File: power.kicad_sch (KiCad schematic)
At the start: 1 part, among them U5 INA226

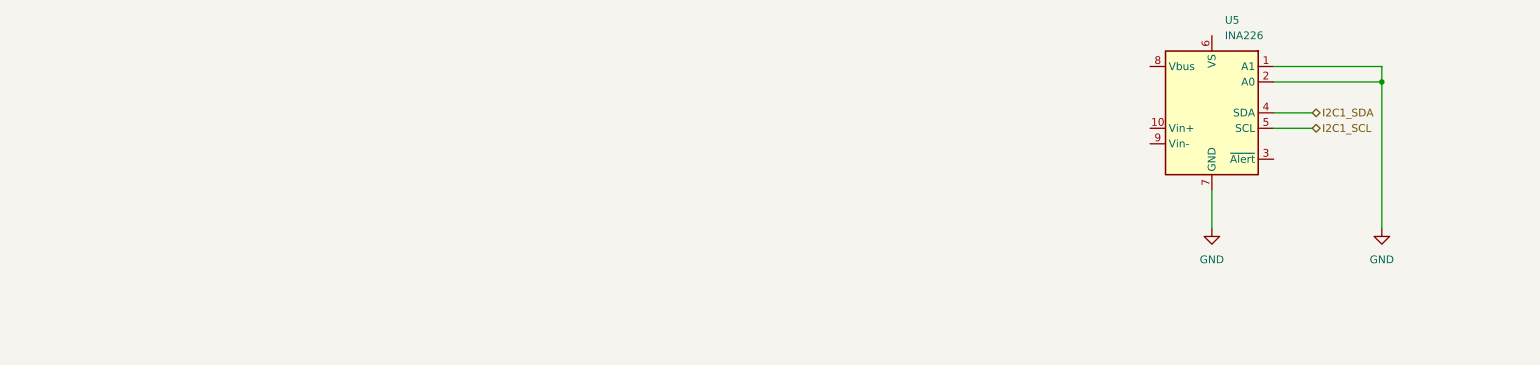
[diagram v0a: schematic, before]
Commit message: added main buck to step Vbat to 5V
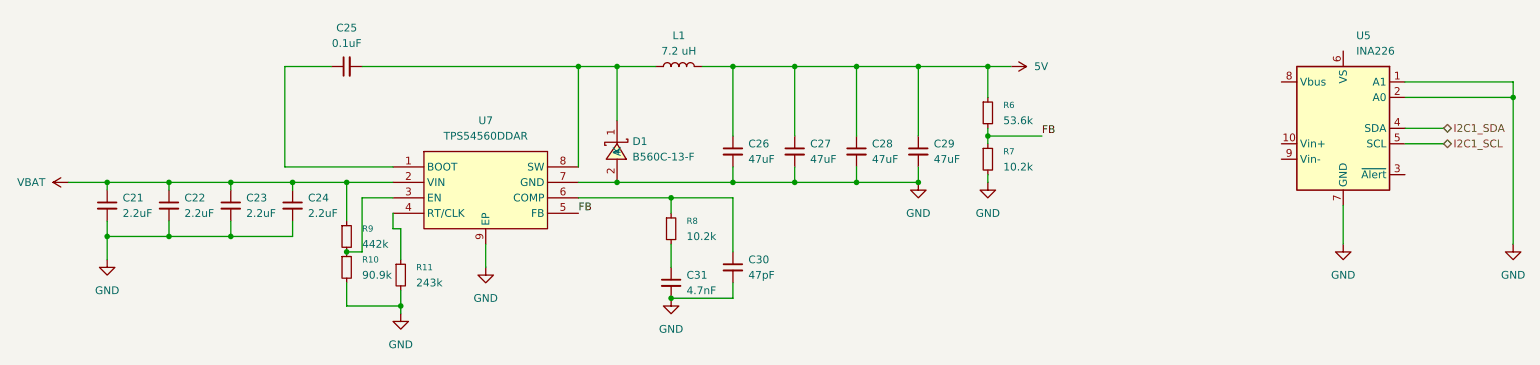
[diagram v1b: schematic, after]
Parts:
- added C21, C22, C23, C24: 2.2uF, Capacitor_SMD:C_0201_0603Metric_Pad0.64x0.40mm_HandSolder, symbol Device:C_Small
- added C25: 0.1uF, Capacitor_SMD:C_0201_0603Metric_Pad0.64x0.40mm_HandSolder, symbol Device:C_Small
- added C26, C27, C28, C29: 47uF, Capacitor_SMD:C_0201_0603Metric_Pad0.64x0.40mm_HandSolder, symbol Device:C_Small
- added C30: 47pF, Capacitor_SMD:C_0201_0603Metric_Pad0.64x0.40mm_HandSolder, symbol Device:C_Small
- added C31: 4.7nF, Capacitor_SMD:C_0201_0603Metric_Pad0.64x0.40mm_HandSolder, symbol Device:C_Small
- added D1: B560C-13-F, LCSC:SMC_L7.1-W6.2-LS8.1-RD, symbol LCSC:B560C-13-F
- added L1: 7.2 uH, Inductor_SMD:L_0201_0603Metric, symbol Device:L
- added R10: 90.9k, Resistor_SMD:R_0201_0603Metric, symbol Device:R_Small
- added R11: 243k, Resistor_SMD:R_0201_0603Metric, symbol Device:R_Small
- added R6: 53.6k, Resistor_SMD:R_0201_0603Metric, symbol Device:R_Small
- added R7, R8: 10.2k, Resistor_SMD:R_0201_0603Metric, symbol Device:R_Small
- added R9: 442k, Resistor_SMD:R_0201_0603Metric, symbol Device:R_Small
- added U7: TPS54560DDAR, LCSC:SOIC-8_L5.0-W4.0-P1.27-LS6.0-BL-EP2.0, symbol LCSC:TPS54560DDAR
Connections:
- net GND: now also C21.2, C22.2, C23.2, C24.2, C26.2, C27.2, C28.2, C29.2, C30.2, C31.2, D1.2 (A), R10.2, R11.2, R7.2, U7.7 (GND), U7.9 (EP)
- new net: C31.1, R8.2
- new net: C25.1, U7.1 (BOOT)
- new net: R10.1, R9.2, U7.3 (EN)
- new net: R11.1, U7.4 (RT/CLK)
- new net: C30.1, R8.1, U7.6 (COMP)
- new net: C25.2, D1.1 (K), L1.1, U7.8 (SW)
- new net 5V: C26.1, C27.1, C28.1, C29.1, L1.2, R6.1
- new net FB: R6.2, R7.1, U7.5 (FB)
- new net VBAT: C21.1, C22.1, C23.1, C24.1, R9.1, U7.2 (VIN)
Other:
- moved on the sheet: U5

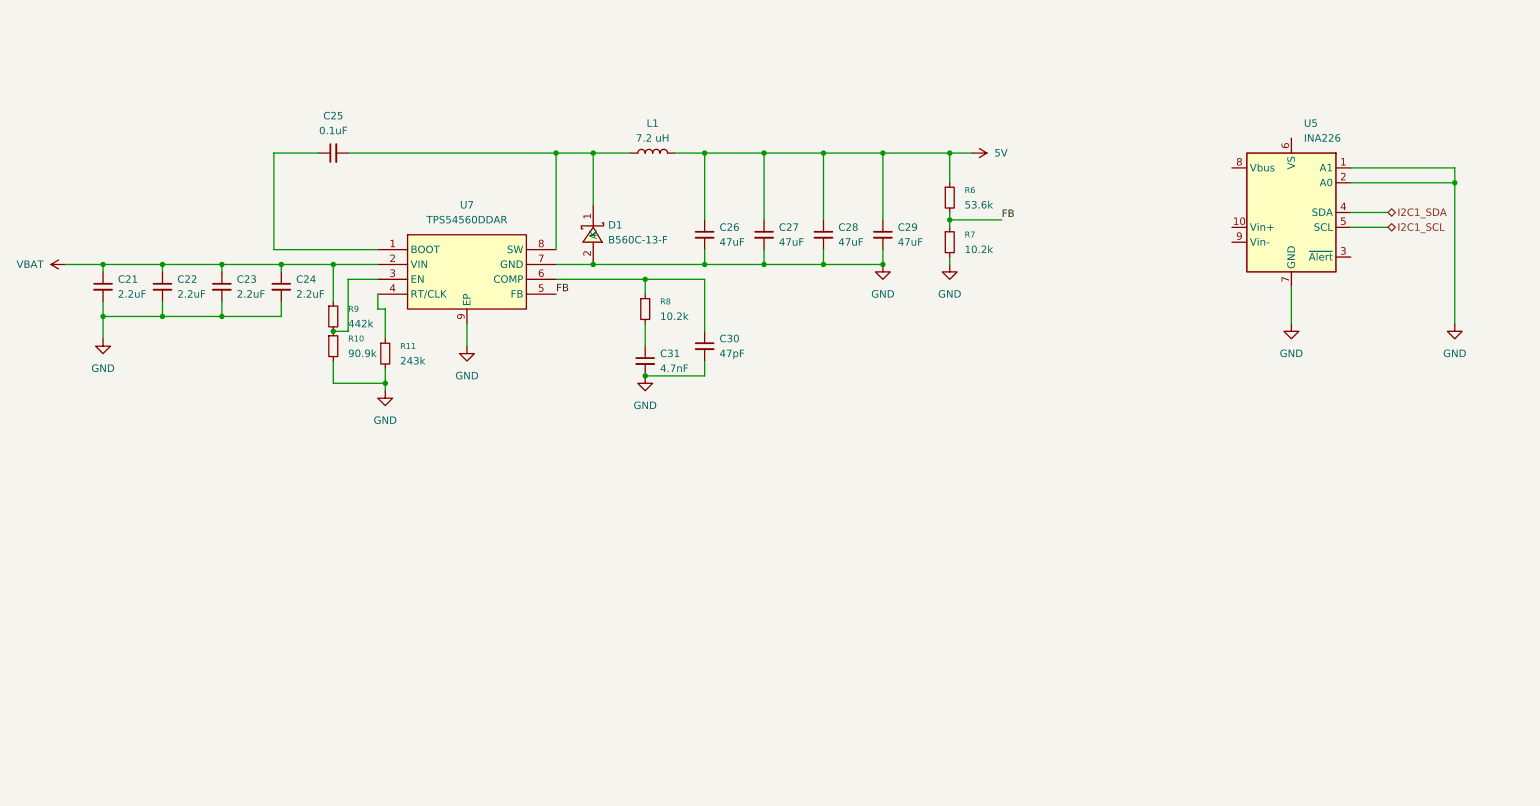
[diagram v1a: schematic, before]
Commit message: added in power converters being LDOs for the sensors and the MCU seperate
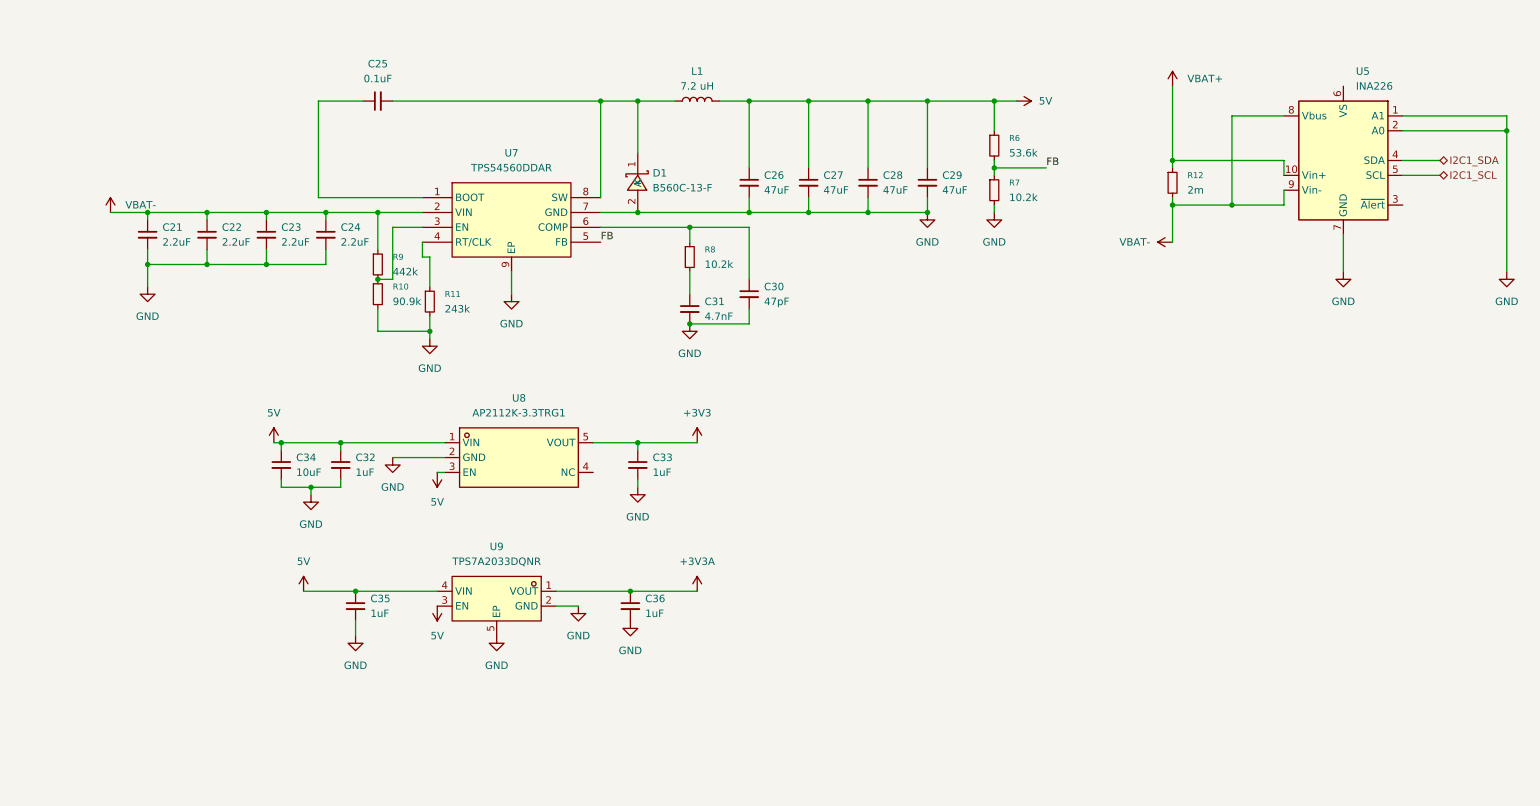
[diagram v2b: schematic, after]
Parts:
- added C32, C33, C35, C36: 1uF, Capacitor_SMD:C_0201_0603Metric_Pad0.64x0.40mm_HandSolder, symbol Device:C_Small
- added C34: 10uF, Capacitor_SMD:C_0201_0603Metric_Pad0.64x0.40mm_HandSolder, symbol Device:C_Small
- added R12: 2m, Resistor_SMD:R_0201_0603Metric, symbol Device:R_Small
- added U8: AP2112K-3.3TRG1, LCSC:SOT-25-5_L2.9-W1.6-P0.95-LS2.8-BL, symbol LCSC:AP2112K-3.3TRG1
- added U9: TPS7A2033DQNR, LCSC:UDFN-4_L1.0-W1.0-P0.65-TL, symbol LCSC:TPS7A2033DQNR
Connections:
- net VBAT is gone; now on net VBAT-: C21.1, C22.1, C23.1, C24.1, R9.1, U7.2 (VIN)
- net 5V: now also C32.1, C34.1, C35.1, U8.1 (VIN), U8.3 (EN), U9.3 (EN), U9.4 (VIN)
- net GND: now also C32.2, C33.2, C34.2, C35.2, C36.2, U8.2 (GND), U9.2 (GND), U9.5 (EP)
- net VBAT+: now reaches U5.10 (Vin+)
- net VBAT+: now also R12.1
- net VBAT-: now reaches U5.8 (Vbus)
- net VBAT-: now also U5.9 (Vin-), R12.2
- new net +3V3: C33.1, U8.5 (VOUT)
- new net +3V3A: C36.1, U9.1 (VOUT)
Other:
- moved on the sheet: C21, C22, C23, C24, C25, C26, C27, C28, C29, C30, C31, D1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

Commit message: Added new connector types for future connections later
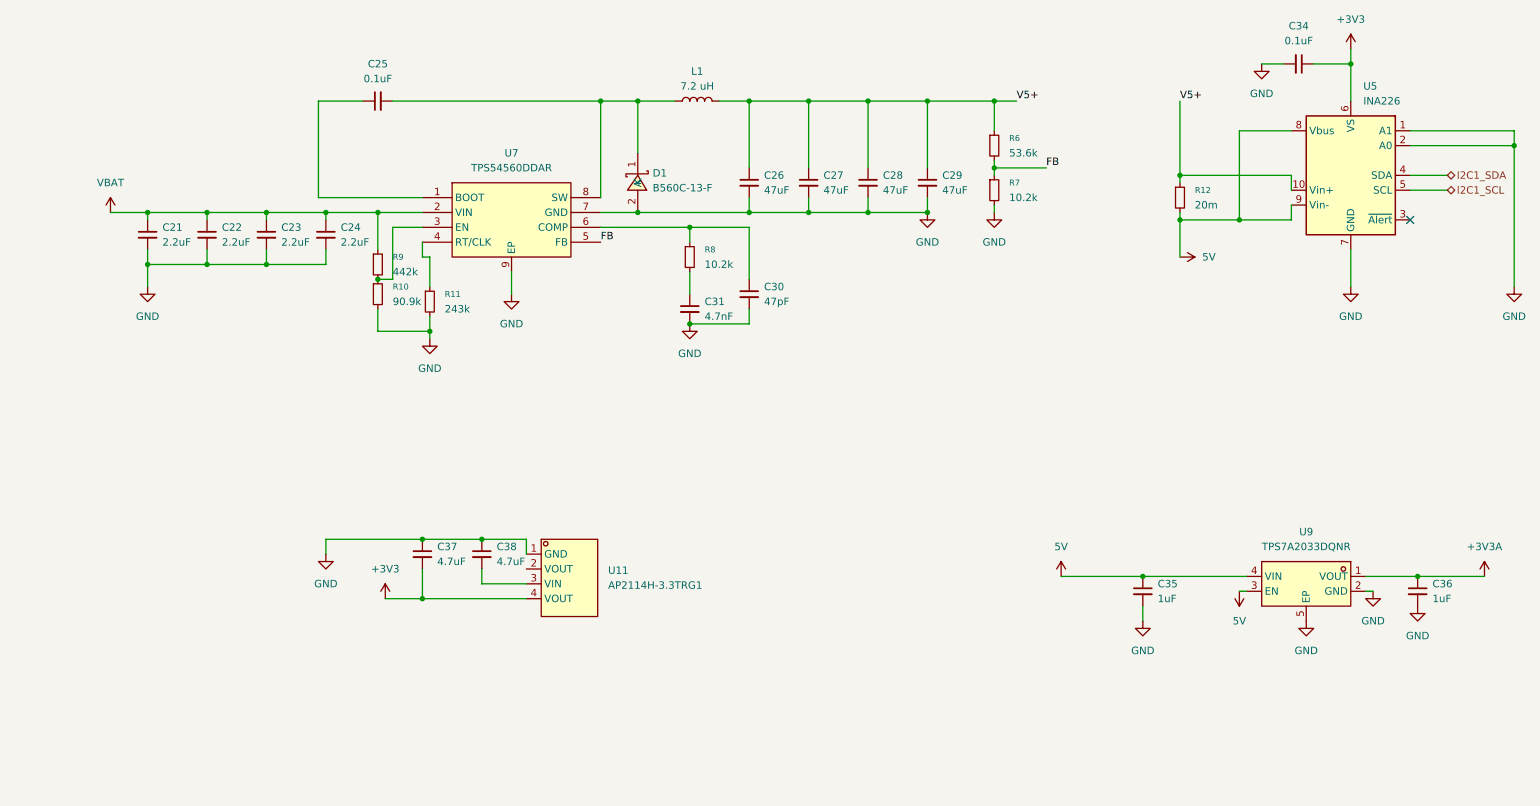
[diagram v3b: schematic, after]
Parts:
- removed C32, C33: 1uF, Capacitor_SMD:C_0201_0603Metric_Pad0.64x0.40mm_HandSolder, symbol Device:C_Small
- removed U8: AP2112K-3.3TRG1, LCSC:SOT-25-5_L2.9-W1.6-P0.95-LS2.8-BL, symbol LCSC:AP2112K-3.3TRG1
- added C37, C38: 4.7uF, Capacitor_SMD:C_0201_0603Metric_Pad0.64x0.40mm_HandSolder, symbol Device:C_Small
- added U11: AP2114H-3.3TRG1, LCSC:SOT-223_L6.7-W3.5-P2.30-BR, symbol LCSC:AP2114H-3.3TRG1
- C34: value 10uF -> 0.1uF
- R12: value 2m -> 20m
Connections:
- net +3V3: now also C34.1, U5.6 (VS), C37.2, U11.4 (VOUT)
- net 5V: now also R12.2, U5.8 (Vbus), U5.9 (Vin-); no longer C26.1, C27.1, C28.1, C29.1, C34.1, L1.2, R6.1
- net GND: now also C37.1, C38.1, U11.1 (GND)
- net VBAT+ renamed V5+
- net V5+: now also C26.1, C27.1, C28.1, C29.1, L1.2, R6.1
- net VBAT- renamed VBAT
- net VBAT: no longer R12.2, U5.8 (Vbus), U5.9 (Vin-)
- new net: C38.2, U11.3 (VIN)
- no-connect marks 0 -> 1
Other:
- moved on the sheet: C35, C36, R12, U5, U9

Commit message: mainly added usart 3, uart 4, and I2C3 connections and planning to add a CAN connection
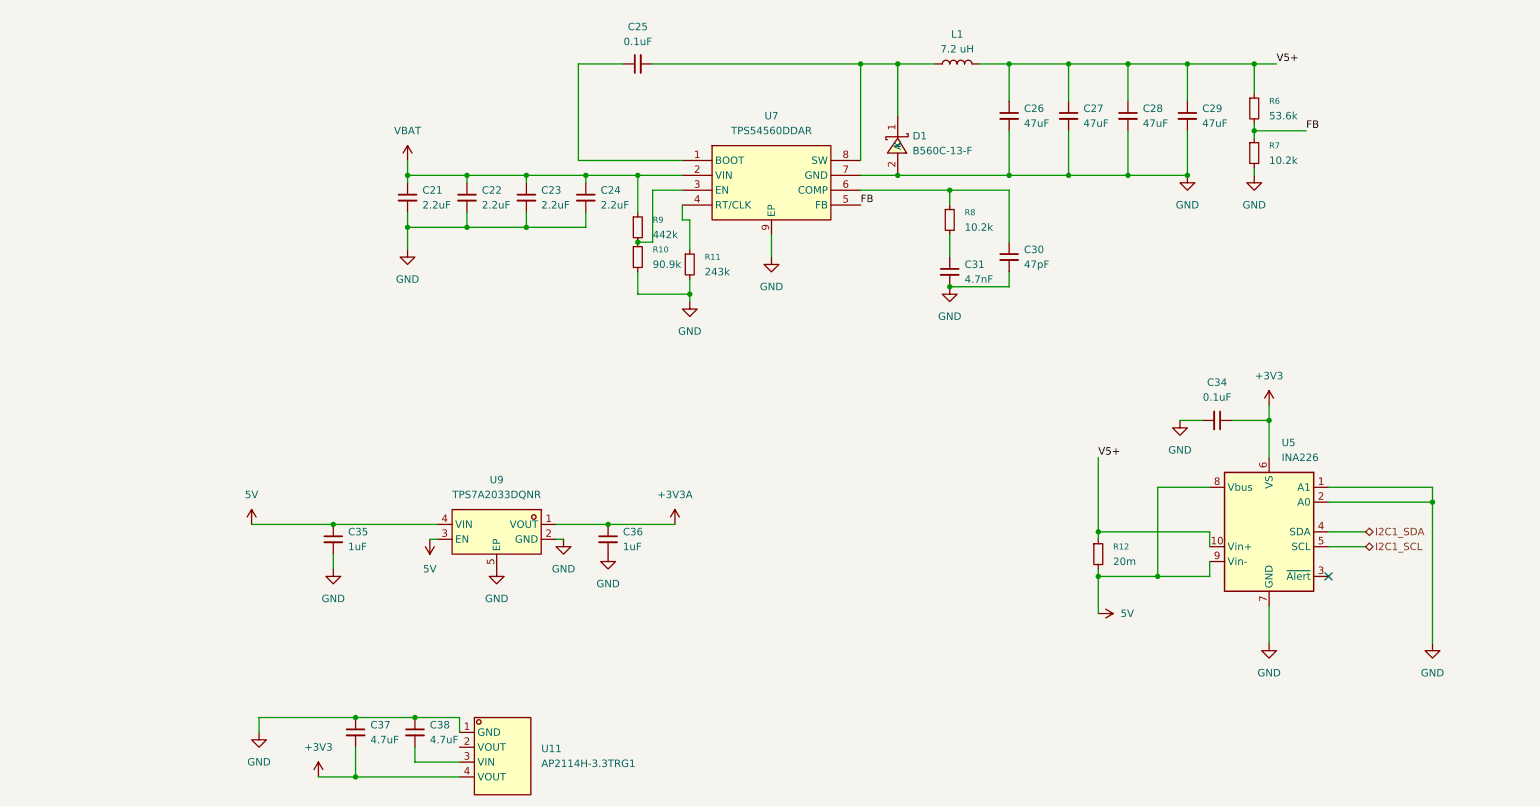
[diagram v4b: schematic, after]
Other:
- moved on the sheet: C21, C22, C23, C24, C25, C26, C27, C28, C29, C30, C31, C34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
